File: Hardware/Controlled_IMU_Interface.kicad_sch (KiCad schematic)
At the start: 1 part, among them J15 Conn_02x07_Odd_Even

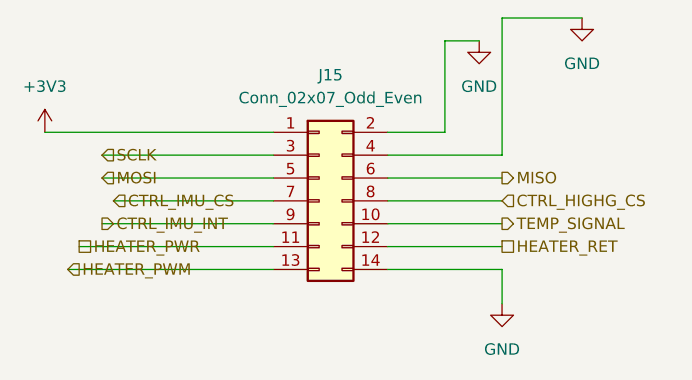
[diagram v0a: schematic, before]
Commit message: Updated Baseboard design but with power supply problems
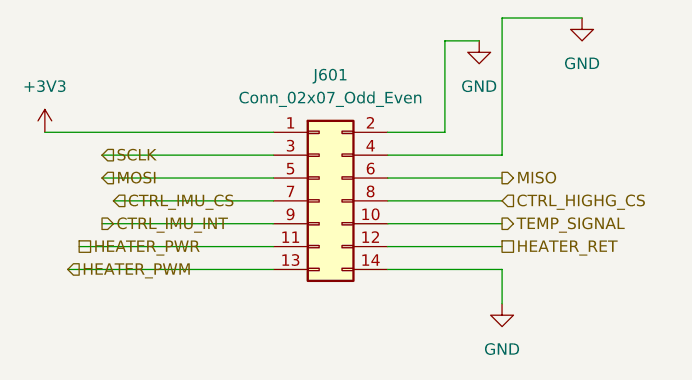
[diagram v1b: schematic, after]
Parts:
- renumbered J15 to J601
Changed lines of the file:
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@@
 		(dnp no)
 		(fields_autoplaced yes)
-		(property "Reference" "#PWR0133"
+		(property "Reference" "#PWR0602"
 			(at 160.02 77.47 0)
 			(effects
@@
 			(project ""
 				(path "/e63e39d7-6ac0-4ffd-8aa3-1841a4541b55/6b287ed4-4ddc-456e-af8d-0328553d2aec"
-					(reference "#PWR0133")
+					(reference "#PWR0602")
 					(unit 1)
 				)
@@
 		(dnp no)
 		(fields_autoplaced yes)
-		(property "Reference" "#PWR0134"
+		(property "Reference" "#PWR0604"
 			(at 171.45 74.93 0)
 			(effects
@@
 			(project ""
 				(path "/e63e39d7-6ac0-4ffd-8aa3-1841a4541b55/6b287ed4-4ddc-456e-af8d-0328553d2aec"
-					(reference "#PWR0134")
+					(reference "#PWR0604")
 					(unit 1)
 				)
@@
 		(dnp no)
 		(fields_autoplaced yes)
-		(property "Reference" "J15"
+		(property "Reference" "J601"
 			(at 143.51 74.93 0)
 			(effects
@@
 			(project ""
 				(path "/e63e39d7-6ac0-4ffd-8aa3-1841a4541b55/6b287ed4-4ddc-456e-af8d-0328553d2aec"
-					(reference "J15")
+					(reference "J601")
 					(unit 1)
 				)
@@
 		(dnp no)
 		(fields_autoplaced yes)
-		(property "Reference" "#PWR0139"
+		(property "Reference" "#PWR0601"
 			(at 111.76 85.09 0)
 			(effects
@@
 			(project ""
 				(path "/e63e39d7-6ac0-4ffd-8aa3-1841a4541b55/6b287ed4-4ddc-456e-af8d-0328553d2aec"
-					(reference "#PWR0139")
+					(reference "#PWR0601")
 					(unit 1)
 				)
@@
 		(dnp no)
 		(fields_autoplaced yes)
-		(property "Reference" "#PWR0140"
+		(property "Reference" "#PWR0603"
 			(at 162.56 106.68 0)
 			(effects
@@
 			(project ""
 				(path "/e63e39d7-6ac0-4ffd-8aa3-1841a4541b55/6b287ed4-4ddc-456e-af8d-0328553d2aec"
-					(reference "#PWR0140")
-					(unit 1)
-				)
+					(reference "#PWR0603")
+					(unit 1)
+				)
